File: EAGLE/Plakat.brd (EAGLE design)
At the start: 82.4 x 68.1 mm, 25 parts, among them X1 USB-MICROB

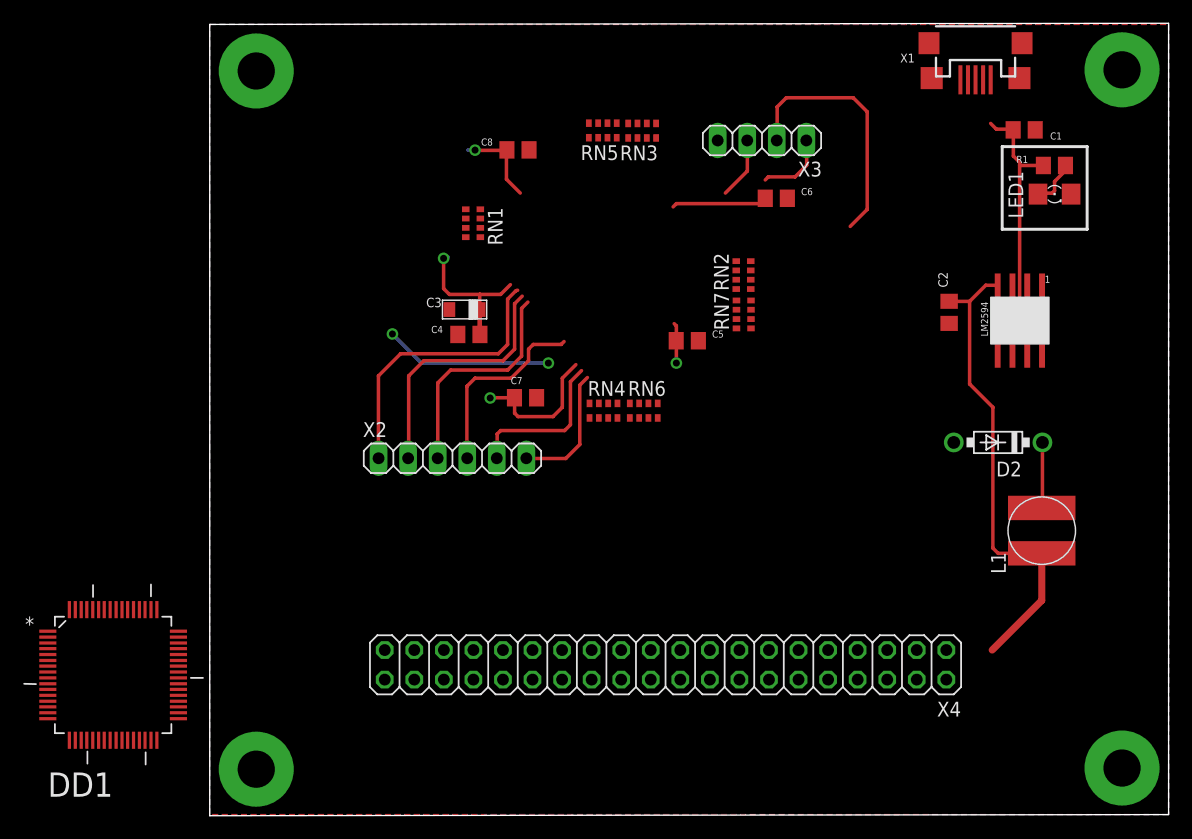
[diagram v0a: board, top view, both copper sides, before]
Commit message: Plakat.sch was redrawed by the right way
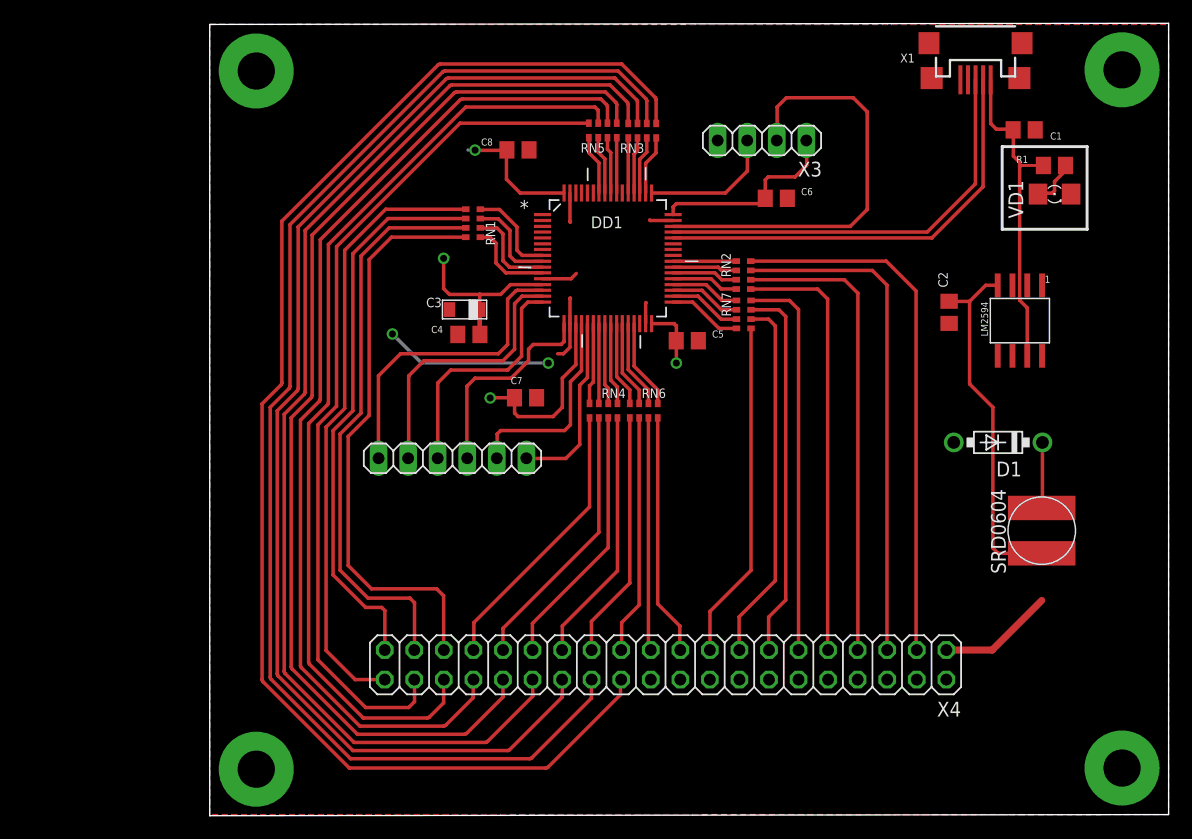
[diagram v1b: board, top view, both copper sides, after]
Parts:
- moved DD1 55.6 mm to (79.6, 56.5)
- renumbered D2 to D1, LED1 to VD1
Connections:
- removed net N$47: RN2.6, X4.8
- removed net N$71: C2.1, C3.+, C4.1, C5.1, C6.1, C7.1, C8.1, DA1.FB, DD1.13, DD1.19, DD1.32, DD1.48, DD1.64, L1.1, X3.1
- new net DM: DD1.44, X1.D-
- new net DP: DD1.45, X1.D+
- new net N$70: RN3.5, X4.24
- new net VCC: C2.1, C3.+, C4.1, C5.1, C6.1, C7.1, C8.1, DA1.FB, DD1.13, DD1.19, DD1.32, DD1.48, DD1.64, L1.1, X3.1, X4.1
- net GND: now also X4.2
- net N$1: now also X1.VBUS; no longer X1.D+
- net N$12: now also DD1.10; no longer DD1.38
- net N$13: now also DD1.11; no longer DD1.37
- net N$14: now also DD1.24; no longer DD1.36
- net N$15: now also DD1.25; no longer DD1.35
- net N$16: now also DD1.37; no longer DD1.34
- net N$17: now also DD1.38; no longer DD1.33
- net N$18: now also DD1.39; no longer DD1.29
- net N$19: now also DD1.40; no longer DD1.28
- net N$20: now also DD1.51; no longer DD1.27
- net N$21: now also RN3.4; no longer RN3.2
- net N$22: now also DD1.22, RN4.4; no longer DD1.26, RN3.1
- net N$23: now also DD1.23, RN4.3; no longer DD1.51, RN4.5
- net N$24: now also DD1.26, RN6.4; no longer DD1.25, RN4.6
- net N$25: now also DD1.27, RN6.3; no longer DD1.52, RN3.5
- net N$26: now also DD1.55, RN5.4; no longer DD1.24, RN6.5
- net N$27: now also DD1.56, RN5.3; no longer DD1.53, RN6.6
- net N$28: now also DD1.57, RN5.2; no longer DD1.23, RN6.7
- net N$29: now also DD1.58, RN5.1; no longer DD1.55, RN5.5
- net N$32: now also DD1.28, RN6.2; no longer DD1.22, RN5.6
- net N$33: now also DD1.29, RN6.1; no longer DD1.56, RN5.7
- net N$34: now also DD1.33, RN7.4; no longer DD1.11, RN5.8
- net N$35: now also DD1.34, RN7.3; no longer DD1.57, RN6.8
- net N$36: now also DD1.35, RN7.2; no longer DD1.10, RN7.5
- net N$37: now also DD1.36, RN7.1; no longer DD1.58, RN7.6
- net N$38: now also RN2.8, X4.3; no longer DD1.9, RN7.7
- net N$39: now also RN2.7, X4.5; no longer DD1.40, RN7.8
- net N$40: now also RN2.6, X4.7; no longer RN1.5, X4.1
- net N$41: now also RN2.5, X4.9; no longer RN1.6, X4.2
- net N$42: now also RN7.8, X4.11; no longer RN1.7, X4.3
- net N$43: now also RN7.7, X4.13; no longer RN1.8, X4.4
- net N$44: now also RN7.6, X4.15; no longer RN4.7, X4.5
- net N$45: now also RN7.5, X4.17; no longer RN4.8, X4.6
- net N$46: now also RN6.8, X4.19; no longer RN2.5, X4.7
- net N$48: now also RN6.7, X4.21; no longer RN2.7, X4.9
- net N$49: now also RN6.6, X4.23; no longer RN2.8, X4.10
- net N$50: now also RN6.5, X4.25; no longer RN3.6, X4.11
- net N$51: now also RN4.8, X4.27; no longer RN3.7, X4.12
- net N$52: now also RN4.7, X4.29; no longer RN3.8, X4.13
- net N$53: now also RN4.6, X4.31; no longer RN4.4, X4.14
- net N$54: now also RN4.5, X4.33; no longer RN4.3, X4.15
- net N$55: now also RN1.8, X4.35; no longer RN3.4, X4.16
- net N$56: now also RN1.7, X4.37; no longer RN6.4, X4.17
- net N$57: now also RN1.6, X4.39; no longer RN6.3, X4.18
- net N$58: now also RN1.5, X4.40; no longer RN6.2, X4.19
- net N$59: now also RN5.8, X4.38; no longer RN5.4, X4.20
- net N$60: now also RN5.7, X4.36; no longer RN5.3, X4.21
- net N$61: now also RN5.6, X4.34; no longer RN5.2, X4.22
- net N$62: now also RN5.5, X4.32; no longer RN5.1, X4.23
- net N$63: now also RN3.8, X4.30; no longer RN6.1, X4.24
- net N$64: now also RN3.7, X4.28; no longer RN7.4, X4.25
- net N$65: now also RN3.6; no longer RN7.3
- net N$66: now also DD1.52, RN3.2; no longer RN7.2, X4.27
- net N$67: now also DD1.53, RN3.1; no longer RN7.1, X4.28
- net N$7: now also DD1.9; no longer DD1.39
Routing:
- net N$70: track 0.00 -> 119.1 mm
- net N$65: track 0.00 -> 113.0 mm
- net N$64: track 0.00 -> 107.0 mm
- net VCC: track 0.00 -> 106.1 mm, vias 0 -> 4
- net N$63: track 0.00 -> 100.9 mm
- net N$62: track 0.00 -> 94.6 mm
- net N$71: track 92.0 -> 0.00 mm, vias 4 -> 0
- net N$61: track 0.00 -> 88.3 mm
- net N$60: track 0.00 -> 82.0 mm
- net N$59: track 0.00 -> 74.4 mm
- net N$58: track 0.00 -> 53.0 mm
- net N$55: track 0.00 -> 50.1 mm
- net N$56: track 0.00 -> 49.4 mm
- net N$57: track 0.00 -> 48.4 mm
- net N$38: track 0.00 -> 46.2 mm
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
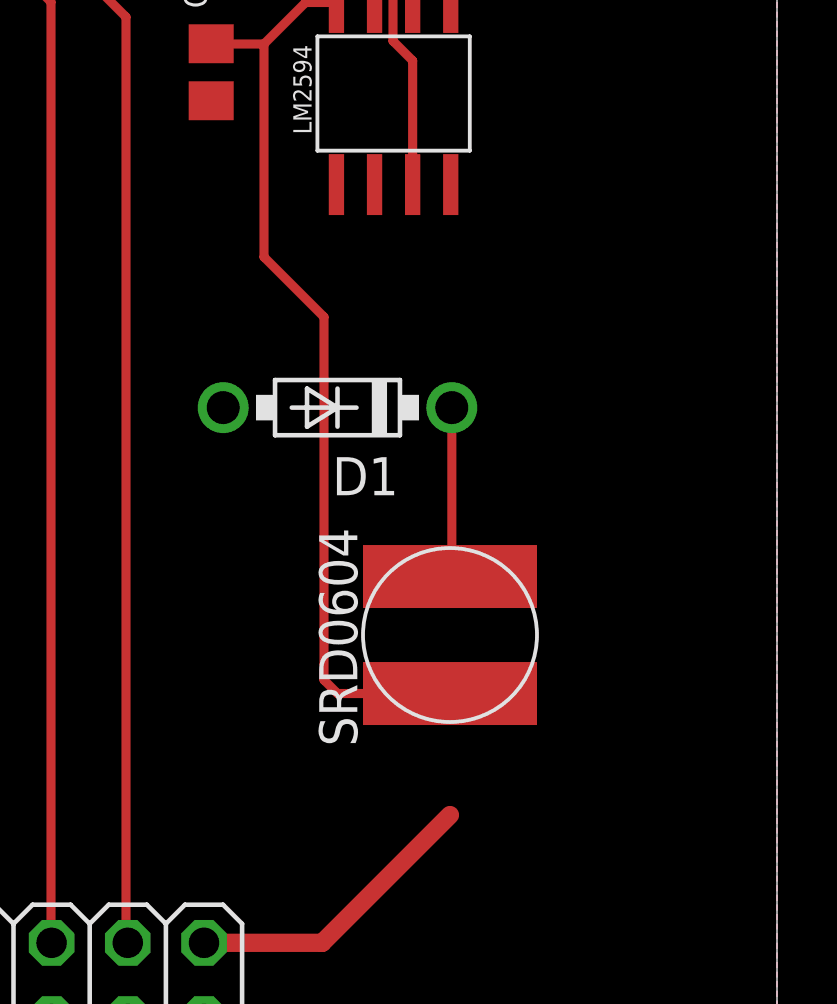
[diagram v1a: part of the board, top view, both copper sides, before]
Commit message: Modified Plakat.brd
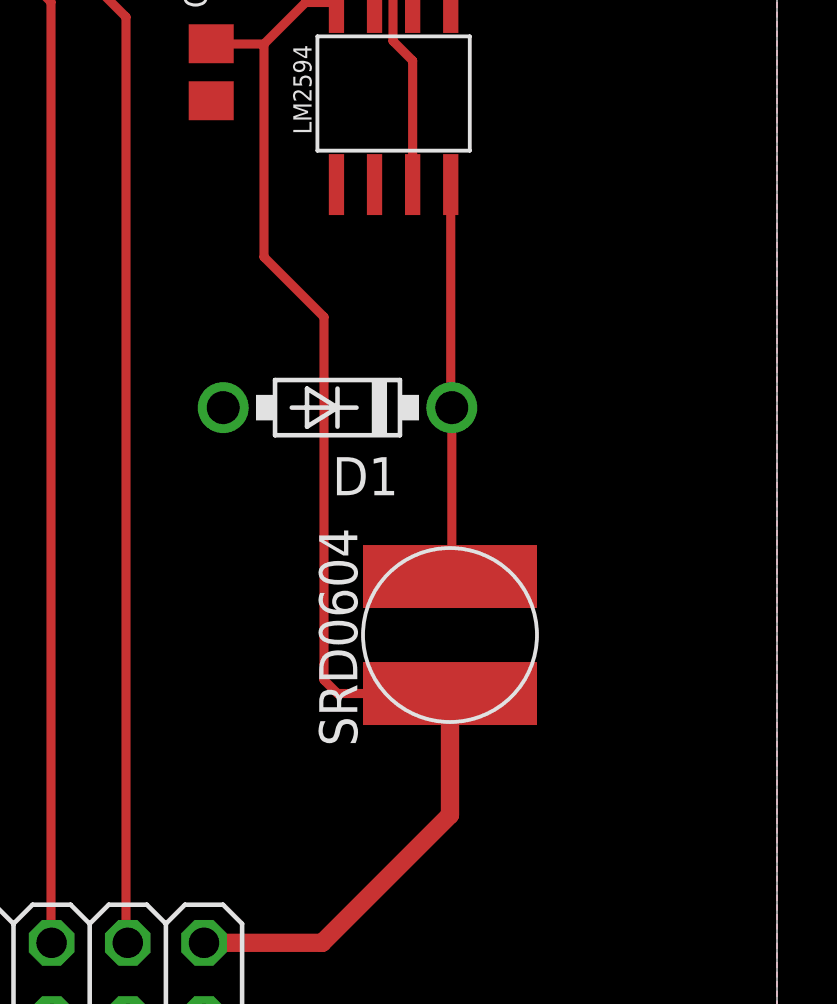
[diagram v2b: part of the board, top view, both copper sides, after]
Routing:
- net N$2: track 5.70 -> 14.7 mm
- net VCC: track 106.1 -> 110.1 mm
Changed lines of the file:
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@@
 <contactref element="L1" pad="2"/>
 <wire x1="116.925" y1="40.715" x2="116.96" y2="40.68" width="0.3048" layer="1"/>
-<wire x1="116.96" y1="40.68" x2="116.96" y2="35.11" width="0.3048" layer="1"/>
 <wire x1="116.96" y1="35.11" x2="116.9" y2="35.05" width="0.3048" layer="1"/>
 <contactref element="DA1" pad="OUT"/>
-<wire x1="116.925" y1="40.715" x2="116.925" y2="48.115" width="0" layer="19" extent="1-1"/>
+<wire x1="116.925" y1="40.715" x2="116.925" y2="48.115" width="0.3048" layer="1"/>
+<wire x1="116.96" y1="40.68" x2="116.96" y2="34.36" width="0.3048" layer="1"/>
+<wire x1="116.96" y1="34.36" x2="116.9" y2="34.3" width="0.3048" layer="1"/>
+<wire x1="116.9" y1="34.3" x2="116.9" y2="35.05" width="0.3048" layer="1"/>
 </signal>
 <signal name="N$1">
@@
 <wire x1="112.7" y1="43.7" x2="110.7" y2="45.7" width="0.3048" layer="1"/>
 <wire x1="110.7" y1="45.7" x2="110.7" y2="52.8" width="0.3048" layer="1"/>
-<wire x1="116.9" y1="27.1" x2="116.9" y2="31.15" width="0" layer="19" extent="1-1"/>
+<wire x1="116.9" y1="27.1" x2="116.9" y2="31.15" width="0.6096" layer="1"/>
 </signal>
 <signal name="N$3">
